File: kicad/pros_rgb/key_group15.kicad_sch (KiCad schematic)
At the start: 16 parts

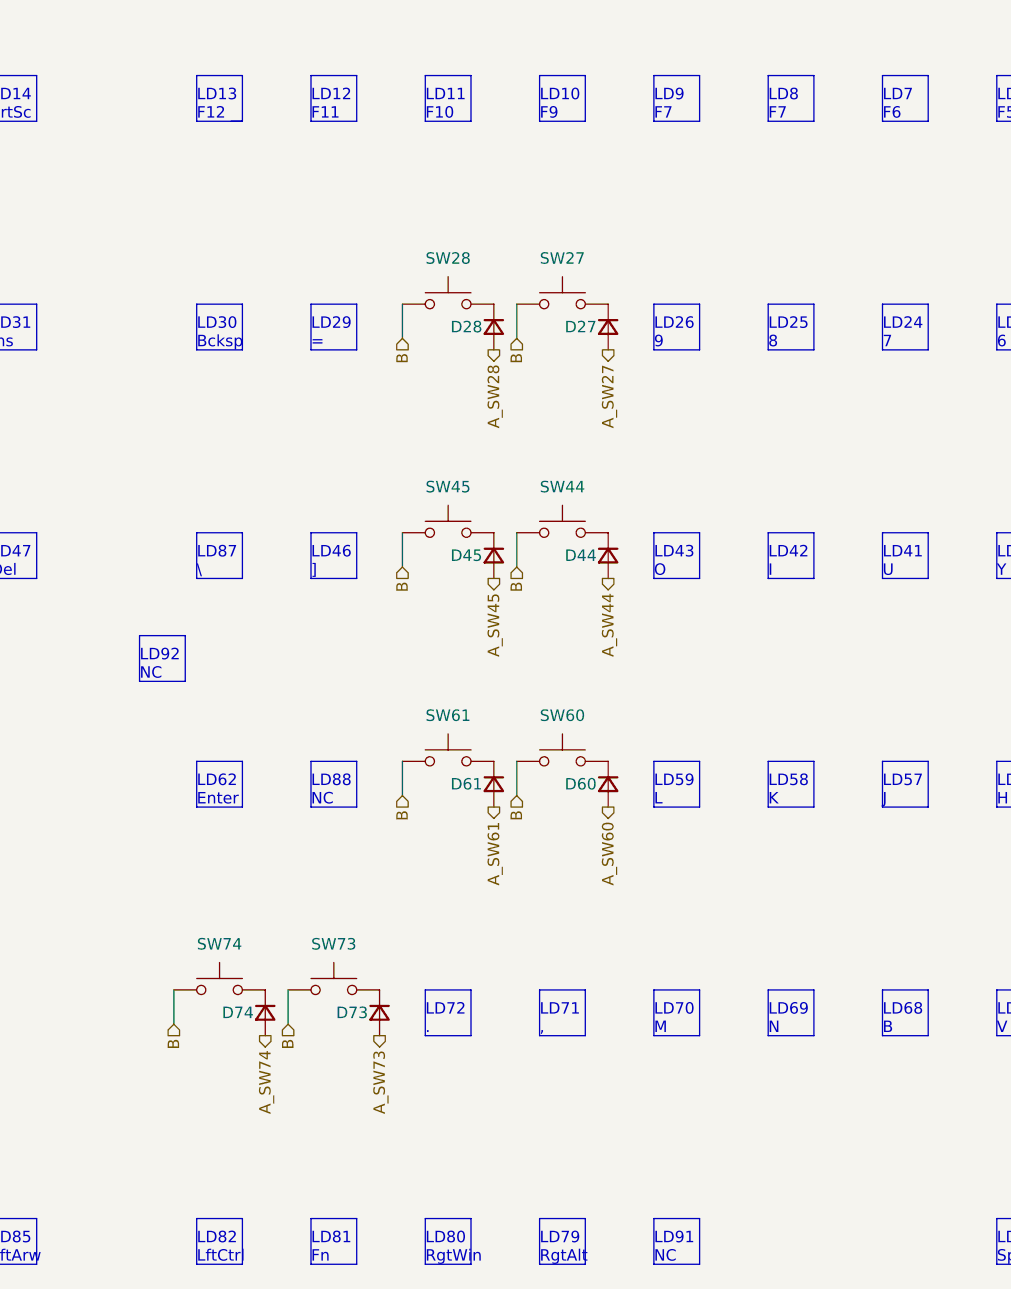
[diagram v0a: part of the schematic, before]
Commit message: kicad/pros_rgb: update key groupings
These new groupings are based off ordering in firmware:
https://github.com/hansemro/pok3r_re_firmware/blob/4b68aa4baf7d28dc8dbf8eebcb1fdb59e7bcd629/disassemble/cmprosrgb/v122/cmprosrgb_v122.txt#L14599-L14629
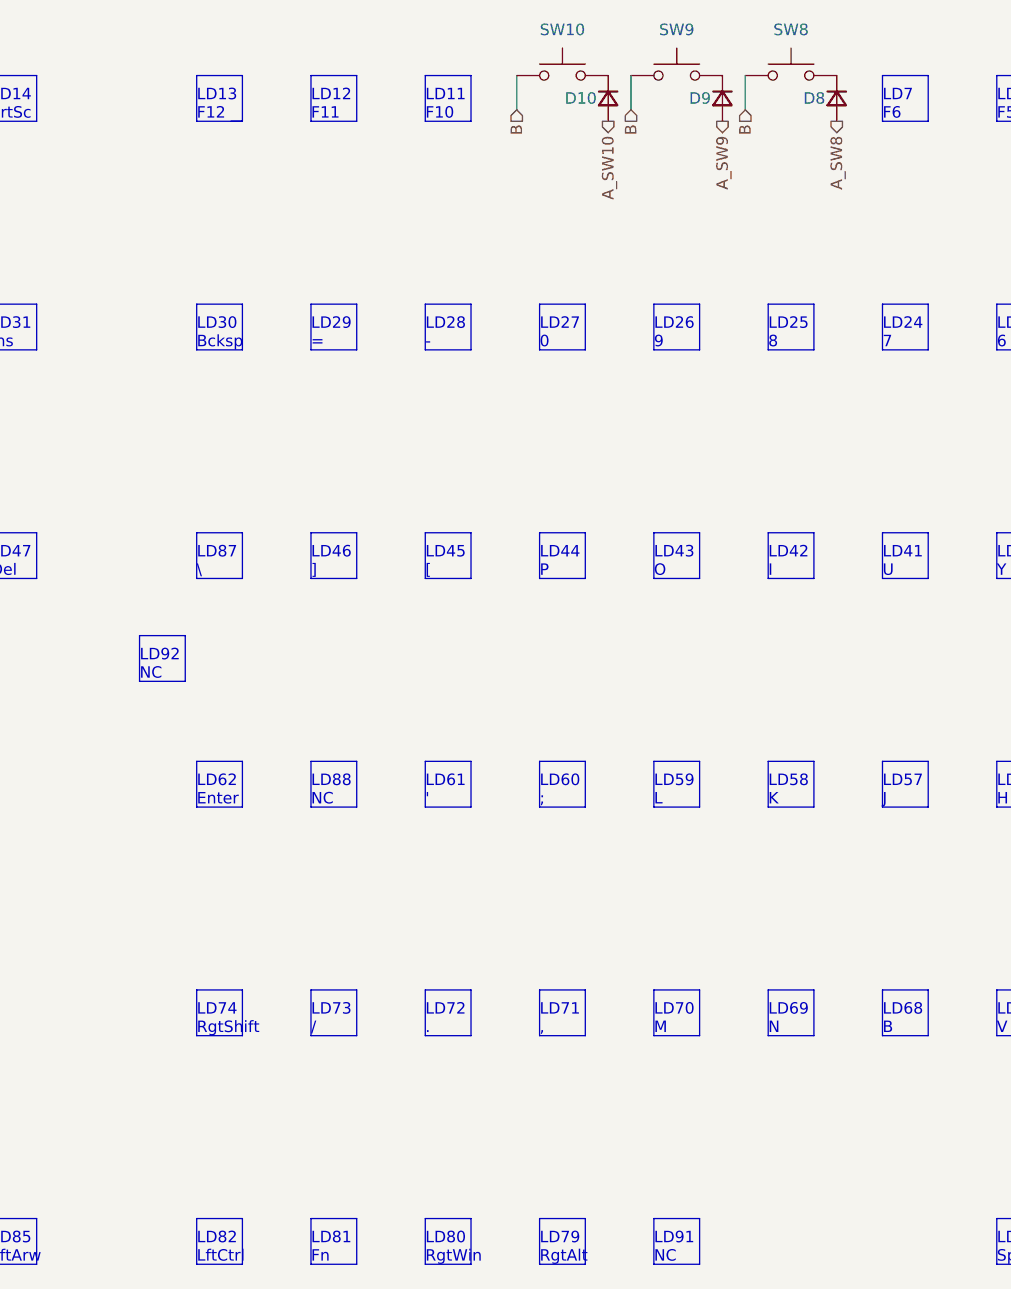
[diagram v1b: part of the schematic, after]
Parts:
- removed D27, D28, D44, D45, D60, D61, D73, D74: ~, symbol Device:D_Small
- removed SW27, SW28, SW44, SW45, SW60, SW61, SW73, SW74: ~, symbol Switch:SW_Push
- added D10, D8, D9: (no value), symbol Device:D_Small
- added SW10, SW8, SW9: (no value), symbol Switch:SW_Push
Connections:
- net B: now also SW10.1, SW8.1, SW9.1
- new net: D9.1 (K), SW9.2
- new net: D10.1 (K), SW10.2
- new net: D8.1 (K), SW8.2
- new net A_SW10: D10.2 (A)
- new net A_SW8: D8.2 (A)
- new net A_SW9: D9.2 (A)
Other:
- note added: "LD27 0"
- note added: "LD28 -"
- note added: "LD44 P"
- note added: "LD45 ["
- note added: "LD60 ;"
- note added: "LD61 '"
- note added: "LD73 /"
- note added: "LD74 RgtShift"
- note removed: "LD10 F9"
- note removed: "LD8 F7"
- note removed: "LD9 F7"

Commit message: kicad/pros_rgb: mark as Rev. B
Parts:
- D10, D8, D9, SW10, SW8, SW9: value (none) -> ~
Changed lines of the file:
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@@
     (in_bom yes) (on_board yes)
     (property "Reference" "SW9" (id 0) (at 160.02 19.05 0))
-    (property "Value" "" (id 1) (at 160.02 19.05 0))
+    (property "Value" "~" (id 1) (at 160.02 19.05 0))
     (property "Footprint" "" (id 2) (at 160.02 19.05 0)
       (effects (font (size 1.27 1.27)) hide)
@@
       (effects (font (size 1.27 1.27)) (justify right))
     )
-    (property "Value" "" (id 1) (at 154.94 27.9399 90)
+    (property "Value" "~" (id 1) (at 154.94 27.9399 90)
       (effects (font (size 1.27 1.27)) (justify left))
     )
@@
       (effects (font (size 1.27 1.27)) (justify right))
     )
-    (property "Value" "" (id 1) (at 180.34 27.9399 90)
+    (property "Value" "~" (id 1) (at 180.34 27.9399 90)
       (effects (font (size 1.27 1.27)) (justify left))
     )
@@
       (effects (font (size 1.27 1.27)) (justify right))
     )
-    (property "Value" "" (id 1) (at 167.64 27.9399 90)
+    (property "Value" "~" (id 1) (at 167.64 27.9399 90)
       (effects (font (size 1.27 1.27)) (justify left))
     )
@@
     (in_bom yes) (on_board yes)
     (property "Reference" "SW10" (id 0) (at 147.32 19.05 0))
-    (property "Value" "" (id 1) (at 147.32 19.05 0))
+    (property "Value" "~" (id 1) (at 147.32 19.05 0))
     (property "Footprint" "" (id 2) (at 147.32 19.05 0)
       (effects (font (size 1.27 1.27)) hide)
@@
     (in_bom yes) (on_board yes)
     (property "Reference" "SW8" (id 0) (at 172.72 19.05 0))
-    (property "Value" "" (id 1) (at 172.72 19.05 0))
+    (property "Value" "~" (id 1) (at 172.72 19.05 0))
     (property "Footprint" "" (id 2) (at 172.72 19.05 0)
       (effects (font (size 1.27 1.27)) hide)

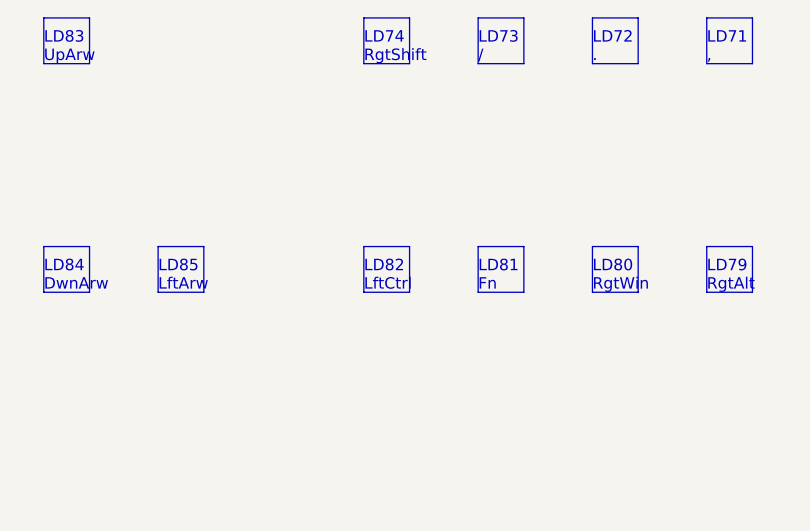
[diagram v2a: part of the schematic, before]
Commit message: kicad/pros_rgb: fix typos
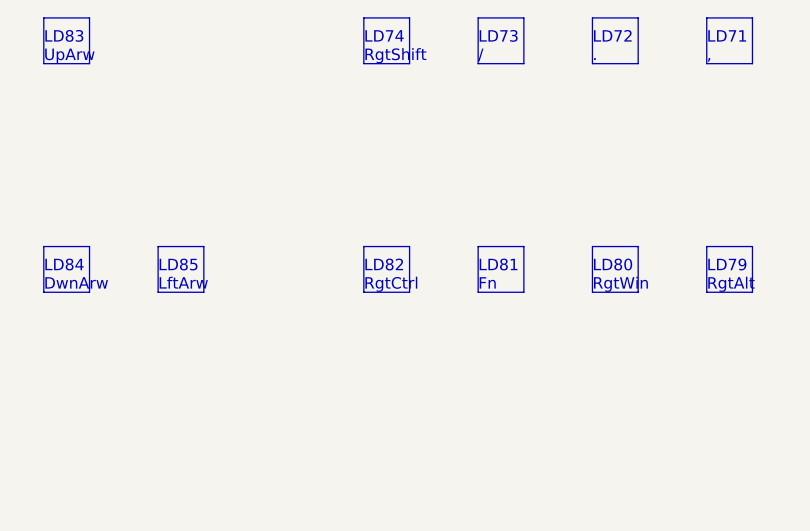
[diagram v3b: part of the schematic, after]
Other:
- note added: "LD82 RgtCtrl"
- note removed: "LD82 LftCtrl"
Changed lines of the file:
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@@
     (effects (font (size 1.27 1.27)) (justify left bottom))
   )
-  (text "LD82\nLftCtrl" (at 106.68 156.21 0)
+  (text "LD82\nRgtCtrl" (at 106.68 156.21 0)
     (effects (font (size 1.27 1.27)) (justify left bottom))
   )
